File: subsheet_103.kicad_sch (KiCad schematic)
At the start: 35 parts, among them T11 BC 547 B

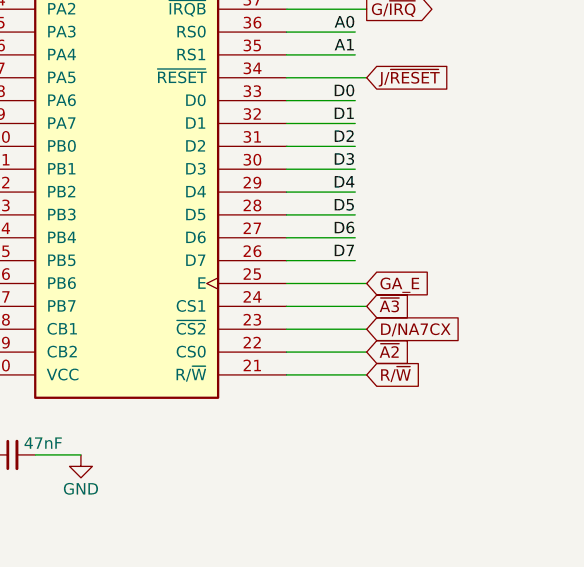
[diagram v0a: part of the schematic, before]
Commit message: rename GA_E/GA_Q/~{GA_E} into E/Q/~{E}
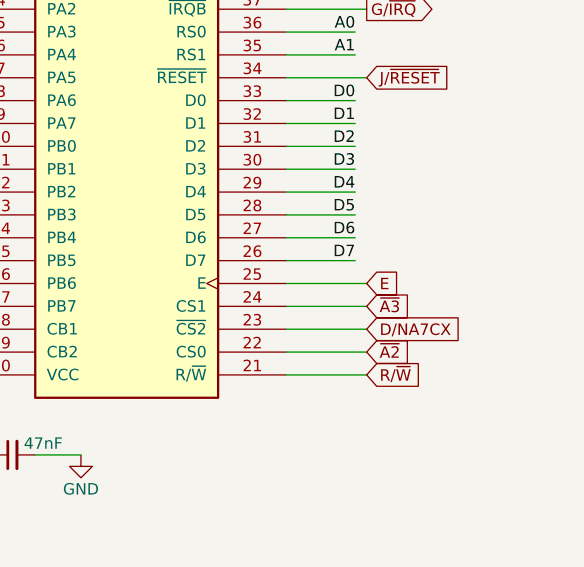
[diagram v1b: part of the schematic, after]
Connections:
- net GA_E renamed E
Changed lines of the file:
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@@
     )
   )
-  (global_label "GA_E" (shape input) (at 177.8 97.79 0) (fields_autoplaced)
+  (global_label "E" (shape input) (at 177.8 97.79 0) (fields_autoplaced)
     (effects (font (size 1.27 1.27)) (justify left))
-    (property "Intersheet References" "${INTERSHEET_REFS}" (id 0) (at 184.6883 97.7106 0)
+    (property "Intersheet References" "${INTERSHEET_REFS}" (id 0) (at 181.3621 97.7106 0)
       (effects (font (size 1.27 1.27)) (justify left) hide)
     )

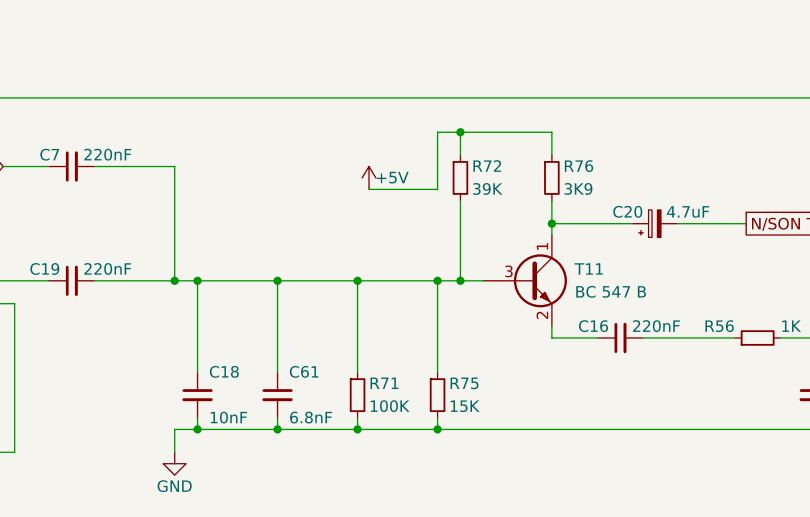
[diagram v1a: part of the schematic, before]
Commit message: Port LEP : report des voltages
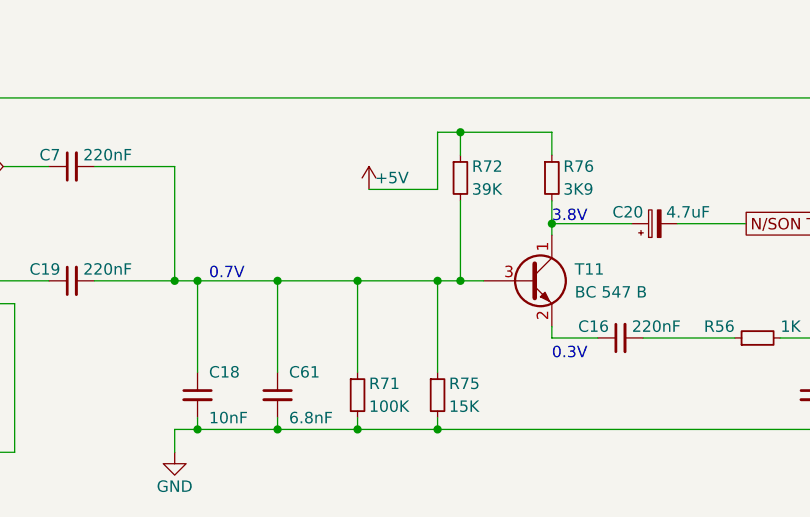
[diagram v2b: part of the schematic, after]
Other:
- note added: "0.3V"
- note added: "0.7V"
- note added: "3.8V"
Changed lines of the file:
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@@
     (stroke (width 0) (type default) (color 0 0 0 0))
+  )
+  (text "0.3V" (at 106.68 242.57 0)
+    (effects (font (size 1.27 1.27)) (justify left bottom))
   )
   (text "de I47-13" (at 132.08 102.87 180)
     (effects (font (size 1.27 1.27)) (justify right bottom))
   )
+  (text "3.8V" (at 106.68 227.33 0)
+    (effects (font (size 1.27 1.27)) (justify left bottom))
+  )
+  (text "0.7V" (at 68.58 233.68 0)
+    (effects (font (size 1.27 1.27)) (justify left bottom))
+  )
   (text "de I45-12" (at 121.92 105.41 0)

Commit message: remise au propre
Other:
- title: Conversion du Thomson MO5 — Unité centrale -> Conversion du Thomson MO5 — Unité centrale v1
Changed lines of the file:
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@@
   (paper "A4" portrait)
   (title_block
-    (title "Conversion du Thomson MO5 — Unité centrale")
-    (date "2023-05-12")
+    (title "Conversion du Thomson MO5 — Unité centrale v1")
+    (date "2023-05-14")
     (rev "DRAFT")
     (comment 1 "http://github.com/sporniket/kicad-conversions--thomson-mo5--v1")
-    (comment 2 "Dépôt d'origine : ")
+    (comment 3 "Gate Array Motorola MCA 1300 ALS")
     (comment 4 "Reference : POP5001 501994-01")
   )
